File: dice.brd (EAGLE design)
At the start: 53.3 x 55.9 mm, 10 parts

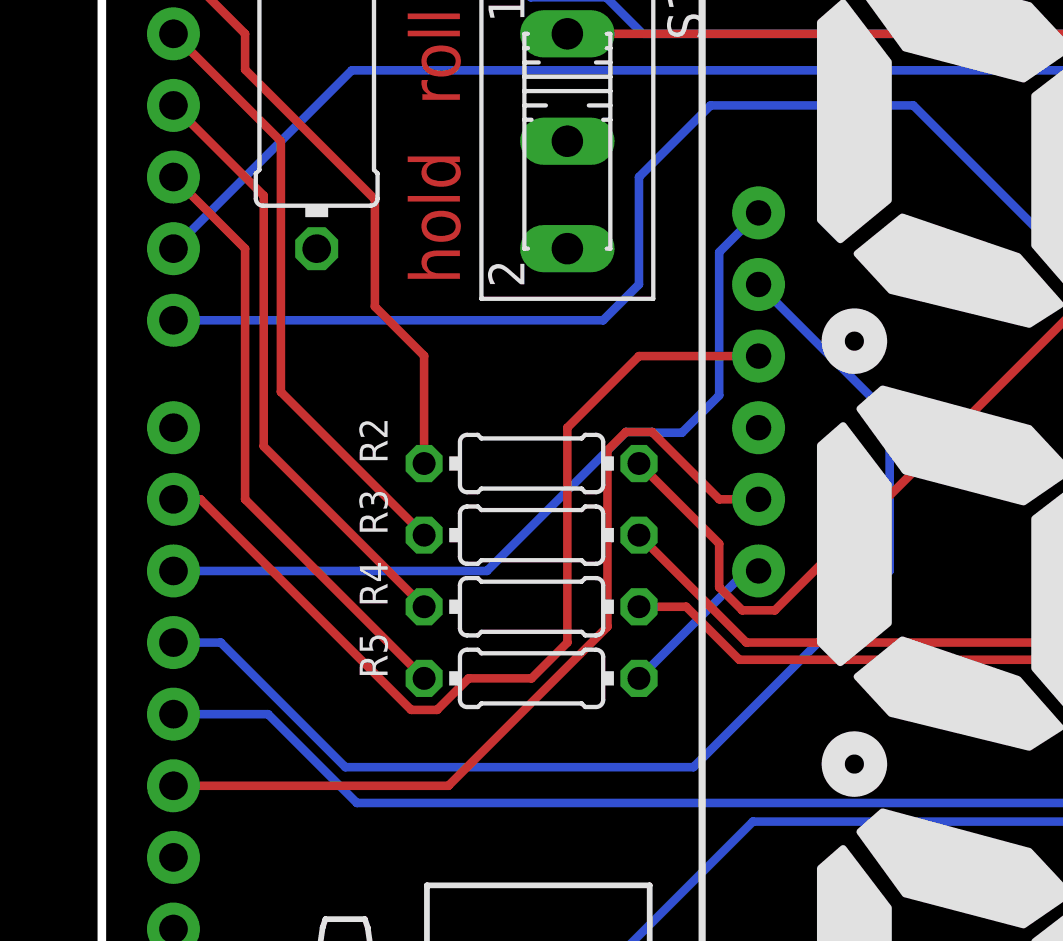
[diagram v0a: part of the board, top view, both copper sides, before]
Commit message: Connect all traces except GND
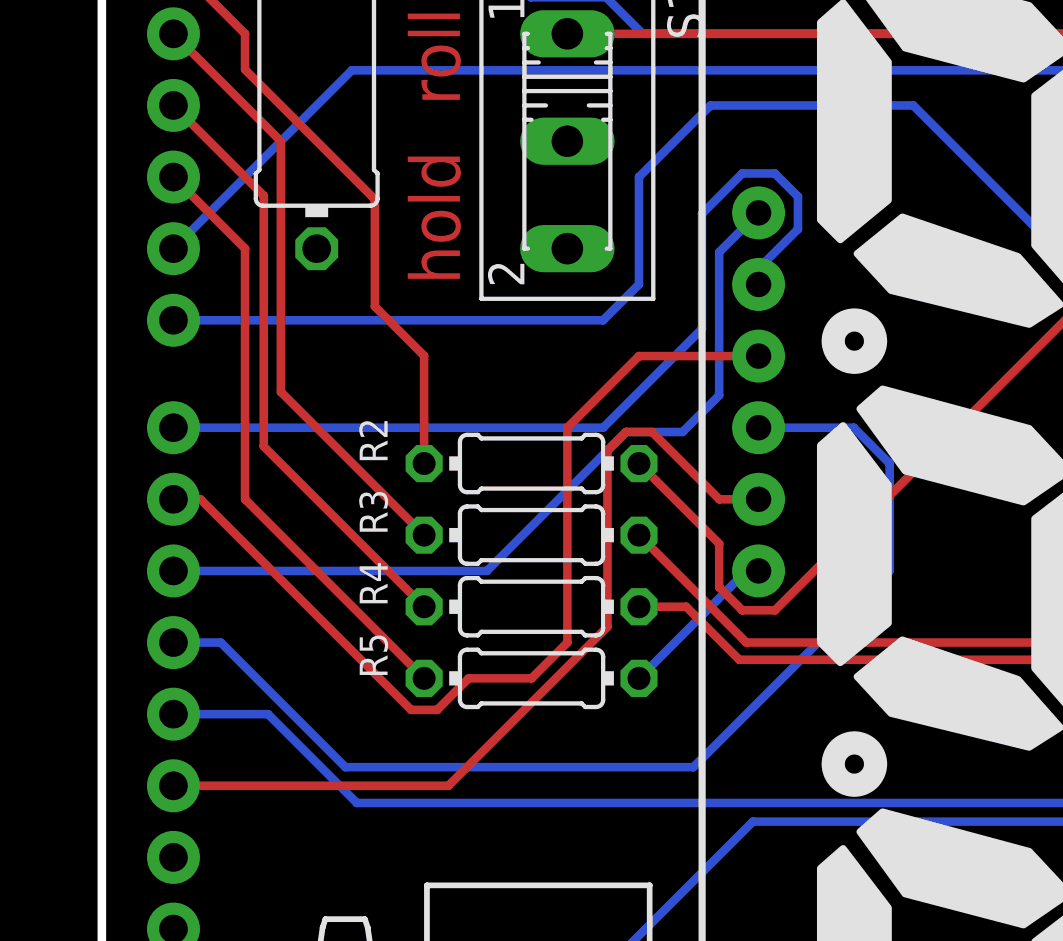
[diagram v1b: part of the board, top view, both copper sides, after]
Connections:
- net N$1 renamed LED
- net C: now also B1.D11; no longer B1.D8
- net D: now also B1.D8, DISP1.2; no longer B1.D13, DISP1.5
- net F: now also B1.D12, DISP1.10; no longer B1.D11, DISP1.2
- net G: now also B1.D13, DISP1.5; no longer B1.D12, DISP1.10
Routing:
- net C: track 0.00 -> 39.1 mm
- net G: track 57.4 -> 30.6 mm
- net F: track 42.2 -> 57.4 mm
- net D: track 30.6 -> 32.3 mm
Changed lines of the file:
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@@
 <wire x1="8.89" y1="50.8" x2="7.62" y2="52.07" width="0.3048" layer="16"/>
 </signal>
-<signal name="N$1">
+<signal name="LED">
 <contactref element="B1" pad="A4"/>
 <contactref element="D1" pad="A"/>
@@
 <wire x1="21.59" y1="43.18" x2="28.7782" y2="43.18" width="0.3048" layer="16"/>
 </signal>
-<signal name="C">
+<signal name="D">
 <contactref element="B1" pad="D8"/>
-<contactref element="DISP1" pad="4"/>
-<wire x1="2.54" y1="31.75" x2="23.2918" y2="31.75" width="0" layer="19" extent="1-1"/>
+<contactref element="DISP1" pad="2"/>
+<wire x1="24.6888" y1="38.7913375" x2="24.6888" y2="39.9486625" width="0.3048" layer="16"/>
+<wire x1="24.6888" y1="39.9486625" x2="23.8704625" y2="40.767" width="0.3048" layer="16"/>
+<wire x1="23.8704625" y1="40.767" x2="22.7131375" y2="40.767" width="0.3048" layer="16"/>
+<wire x1="22.7131375" y1="40.767" x2="21.2852" y2="39.3390625" width="0.3048" layer="16"/>
+<wire x1="21.2852" y1="39.3390625" x2="21.2852" y2="35.2552" width="0.3048" layer="16"/>
+<wire x1="23.2918" y1="36.83" x2="23.2918" y2="37.3943375" width="0.3048" layer="16"/>
+<wire x1="23.2918" y1="37.3943375" x2="24.6888" y2="38.7913375" width="0.3048" layer="16"/>
+<wire x1="17.78" y1="31.75" x2="2.54" y2="31.75" width="0.3048" layer="16"/>
+<wire x1="21.2852" y1="35.2552" x2="17.78" y2="31.75" width="0.3048" layer="16"/>
 </signal>
 <signal name="DP">
@@
 <contactref element="B1" pad="D10"/>
 <contactref element="DISP1" pad="1"/>
-<wire x1="18.58706875" y1="31.5976" x2="19.51293125" y2="31.5976" width="0.3048" layer="16"/>
-<wire x1="19.51293125" y1="31.5976" x2="19.53833125" y2="31.5722" width="0.3048" layer="16"/>
-<wire x1="19.53833125" y1="31.5722" x2="20.57250625" y2="31.5722" width="0.3048" layer="16"/>
+<wire x1="18.58706875" y1="31.5976" x2="20.59790625" y2="31.5976" width="0.3048" layer="16"/>
 <wire x1="2.54" y1="26.67" x2="13.65946875" y2="26.67" width="0.3048" layer="16"/>
 <wire x1="13.65946875" y1="26.67" x2="18.58706875" y2="31.5976" width="0.3048" layer="16"/>
-<wire x1="20.57250625" y1="31.5722" x2="21.8948" y2="32.89449375" width="0.3048" layer="16"/>
+<wire x1="20.59790625" y1="31.5976" x2="21.8948" y2="32.89449375" width="0.3048" layer="16"/>
 <wire x1="21.8948" y1="37.973" x2="23.2918" y2="39.37" width="0.3048" layer="16"/>
 <wire x1="21.8948" y1="32.89449375" x2="21.8948" y2="37.973" width="0.3048" layer="16"/>
 </signal>
-<signal name="F">
+<signal name="C">
 <contactref element="B1" pad="D11"/>
 <wire x1="2.54" y1="24.13" x2="4.21789375" y2="24.13" width="0.3048" layer="16"/>
 <wire x1="4.21789375" y1="24.13" x2="8.63749375" y2="19.7104" width="0.3048" layer="16"/>
 <wire x1="8.63749375" y1="19.7104" x2="20.9804" y2="19.7104" width="0.3048" layer="16"/>
-<wire x1="27.94" y1="26.67" x2="20.9804" y2="19.7104" width="0.3048" layer="16"/>
-<contactref element="DISP1" pad="2"/>
-<wire x1="23.2918" y1="36.83" x2="27.94" y2="32.1818" width="0.3048" layer="16"/>
-<wire x1="27.94" y1="32.1818" x2="27.94" y2="26.67" width="0.3048" layer="16"/>
+<wire x1="20.9804" y1="19.7104" x2="27.94" y2="26.67" width="0.3048" layer="16"/>
+<contactref element="DISP1" pad="4"/>
+<wire x1="27.94" y1="26.67" x2="27.94" y2="30.48" width="0.3048" layer="16"/>
+<wire x1="27.94" y1="30.48" x2="26.67" y2="31.75" width="0.3048" layer="16"/>
+<wire x1="26.67" y1="31.75" x2="23.2918" y2="31.75" width="0.3048" layer="16"/>
 </signal>
-<signal name="G">
+<signal name="F">
 <contactref element="B1" pad="D12"/>
 <contactref element="DISP1" pad="10"/>
@@
 <wire x1="9.0453875" y1="18.4404" x2="39.0342625" y2="18.4404" width="0.3048" layer="16"/>
 </signal>
-<signal name="D">
+<signal name="G">
 <contactref element="B1" pad="D13"/>
 <contactref element="DISP1" pad="5"/>

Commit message: Add GND pours
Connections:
- net GND: no longer B1.GND@0, B1.GND@1
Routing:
- net SW: track 36.2 -> 37.4 mm
- net POT: track 58.8 -> 59.9 mm
- added copper zone on layer 1, net GND
- added copper zone on layer 16, net GND
- removed copper zone on layer 1, net N$2
- removed copper zone on layer 16, net N$2
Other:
- board text added: "h"
- board text added: "r"
- board text removed: "hold"
- board text removed: "roll"

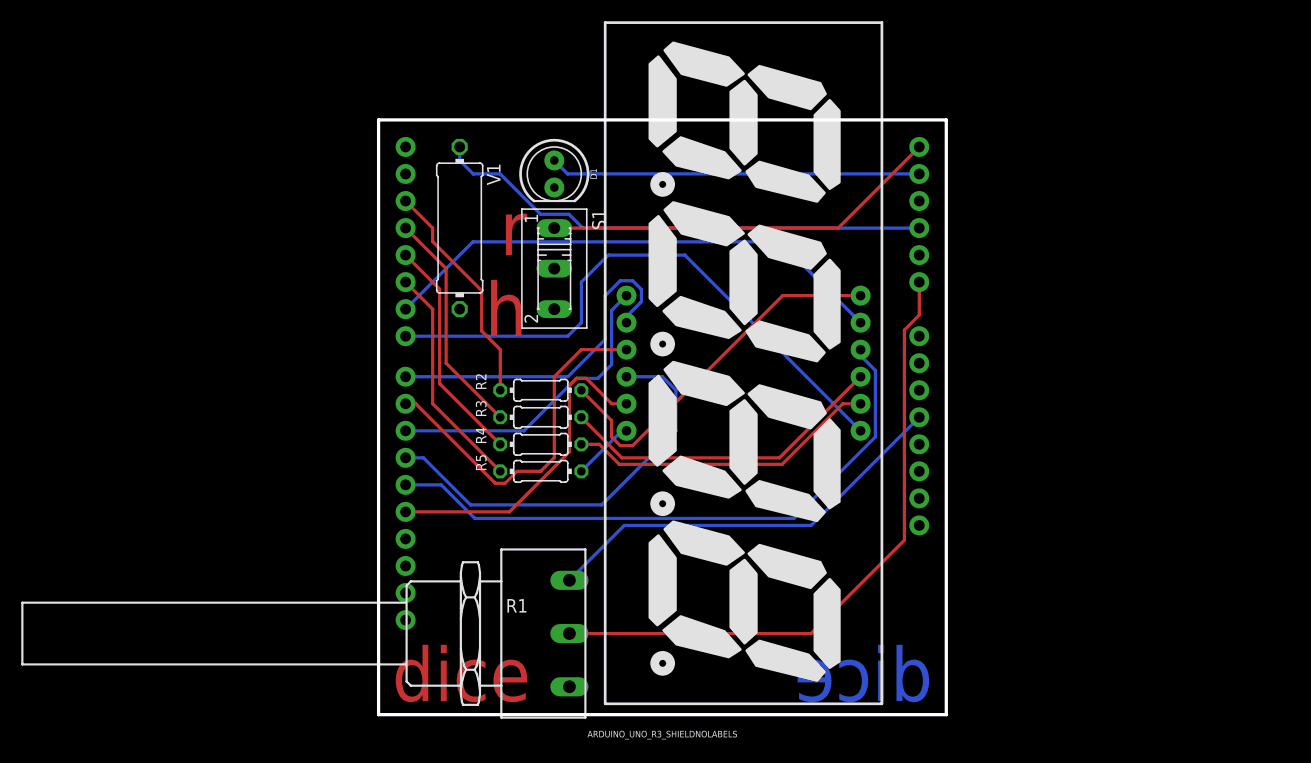
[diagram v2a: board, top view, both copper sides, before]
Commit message: Redo PCB for milling
Switch to one layer

Remove ground pours

Switch to 30mil trace width

Add circles of trace around every pad

Reduce hole size on shield and 7 segment display
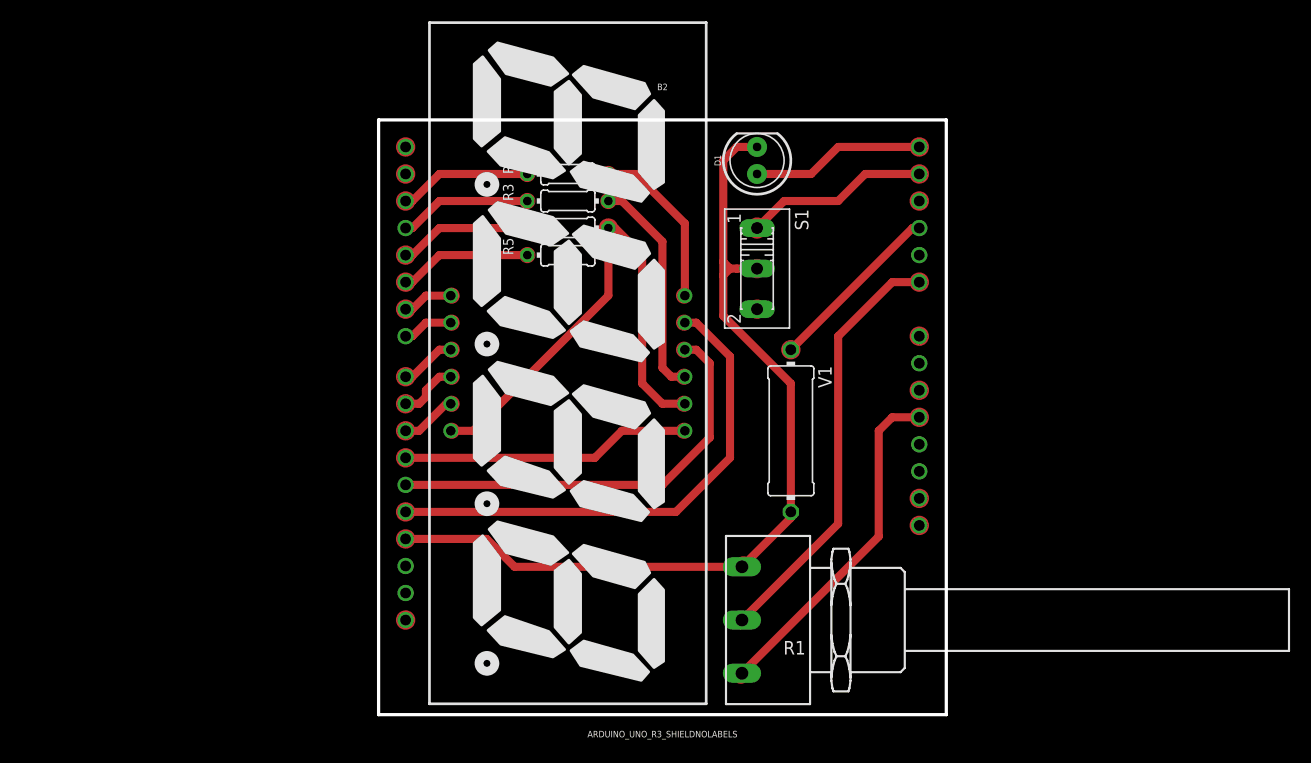
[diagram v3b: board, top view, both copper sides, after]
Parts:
- removed B1: ARDUINO_UNO_R3_SHIELDNOLABELS, SparkFun-Boards:UNO_R3_SHIELD_NOLABELS
- added B2: ARDUINO_UNO_R3_SHIELDNOLABELS, SparkFun-Boards-mtr:UNO_R3_SHIELD_NOLABELS
- DISP1: device SparkFun-LED:7-SEGMENT-4DIGIT-20MM -> SparkFun-LED-mtr:7-SEGMENT-4DIGIT-20MM
- moved V1 36.5 mm to (38.7, 26.7)
- moved R1 29.2 mm to (40.6, 8.89), turned to 90 degrees
- moved R4 20.5 mm to (17.8, 45.7)
- moved R5 20.5 mm to (17.8, 43.2)
- moved R2 20.5 mm to (17.8, 50.8)
- moved R3 20.5 mm to (17.8, 48.3)
- moved D1 19.1 mm to (35.6, 52.1), turned to 90 degrees
- moved S1 19.1 mm to (35.6, 41.9)
- moved DISP1 16.5 mm to (17.8, 33.0)
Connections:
- net A: now also B2.D13; no longer B1.D6
- net B: now also B2.D11; no longer B1.D7
- net C: now also B2.D9; no longer B1.D11
- net D: now also B2.D7; no longer B1.D8
- net D1G: now also B2.D2; no longer B1.D2
- net D2G: now also B2.D3; no longer B1.D3
- net D3G: now also B2.D4; no longer B1.D4
- net D4G: now also B2.D5; no longer B1.D5
- net DP: now also B2.D8; no longer B1.D9
- net E: now also B2.D6; no longer B1.D10
- net F: now also B2.D12; no longer B1.D12
- net G: now also B2.D10; no longer B1.D13
- net GND: now also B2.GND@2; no longer B1.GND@2
- net LED: now also B2.A5; no longer B1.A4
- net POT: now also B2.A0; no longer B1.A0
- net SW: now also B2.A4; no longer B1.A5
- net VCC: now also B2.5V; no longer B1.5V
- net VIBR: now also B2.A2; no longer B1.A2
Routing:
- net GND: track 0.00 -> 83.4 mm
- net C: track 39.1 -> 5.67 mm
- net VIBR: track 47.1 -> 16.8 mm
- net DP: track 33.5 -> 5.29 mm
- net B: track 55.0 -> 27.3 mm
- net D: track 32.3 -> 4.77 mm
- net G: track 30.6 -> 5.29 mm
- net E: track 29.0 -> 4.77 mm
- net SW: track 37.4 -> 17.3 mm
- net POT: track 59.9 -> 40.1 mm
- net D1: track 35.1 -> 15.9 mm
- net LED: track 34.8 -> 16.3 mm
- net D4: track 5.82 -> 23.9 mm
- net F: track 57.4 -> 40.3 mm
- net D2: track 31.0 -> 21.0 mm
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- removed copper zone on layer 16, net GND
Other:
- board text removed: "dice"
- board text removed: "h"
- board text removed: "r"
